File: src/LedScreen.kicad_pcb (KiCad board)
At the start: 2 copper layers, 87 x 84 mm, 38 parts

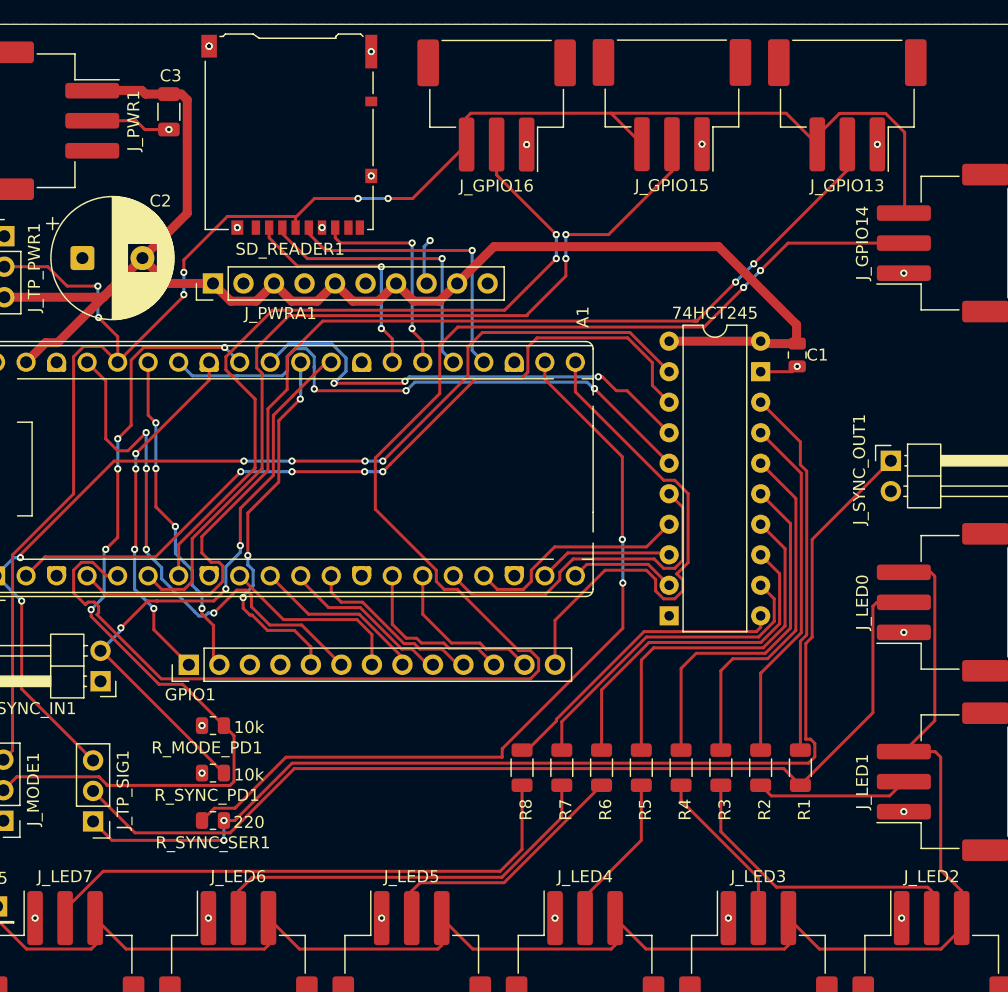
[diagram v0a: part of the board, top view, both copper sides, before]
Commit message: Reorganize KiCad project layout
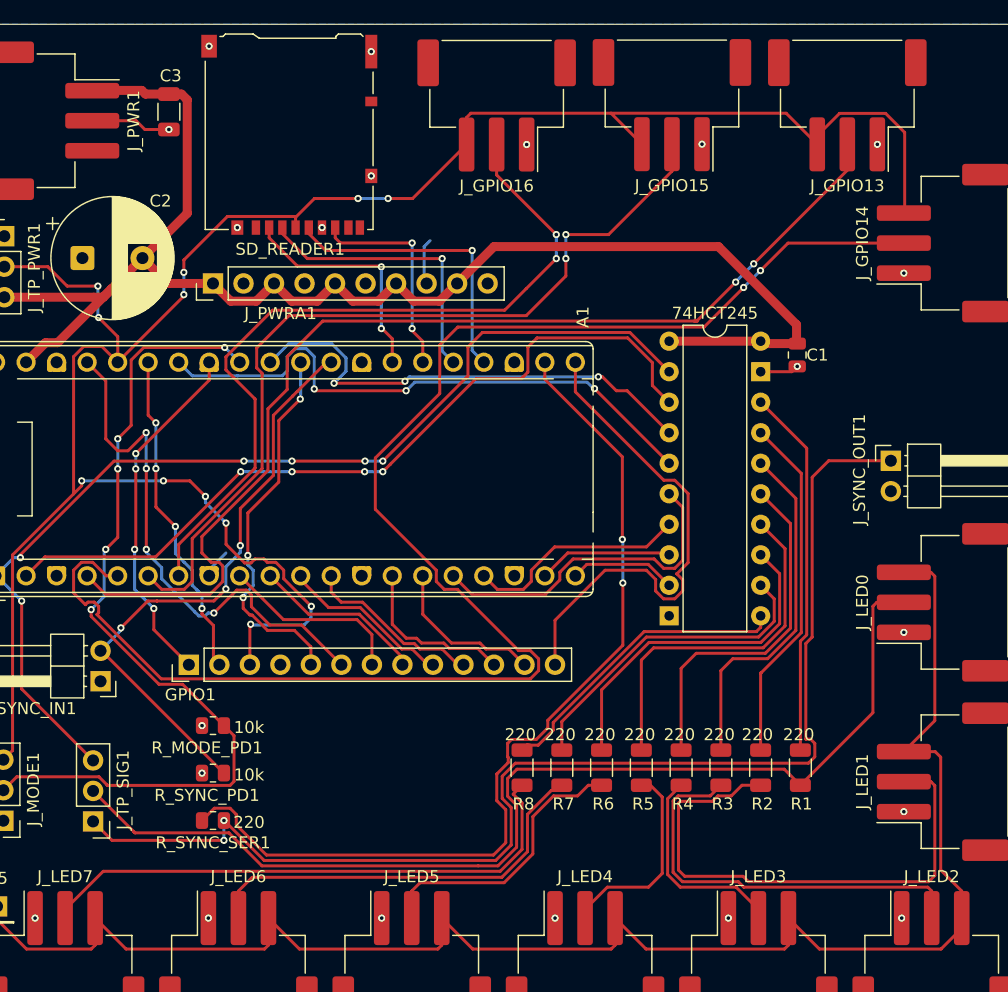
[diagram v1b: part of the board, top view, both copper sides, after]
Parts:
- R1, R2, R3, R4, R5, R6, R7, R8: value 0R -> 220
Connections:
- GPIO1 pad 3: SWCLK -> +3V3
- GPIO1 pad 4: SWDIO -> GND
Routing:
- net +3V3: track 147.7 -> 184.2 mm, vias 6 -> 12
- net LED1_DATA: track 12.8 -> 45.2 mm
- net SYNC_OUT: track 92.8 -> 103.0 mm
- net SYNC_OUT_DRV: track 66.9 -> 76.8 mm
- net LED2_DATA: track 25.7 -> 34.9 mm
- net LED0_DATA: track 83.2 -> 90.0 mm
- net LED4_DATA: track 13.0 -> 16.9 mm
- net LED3_DATA: track 13.7 -> 17.4 mm
- net GND: track 13.9 -> 16.4 mm, vias 23 -> 21
- net LED5_DATA: track 21.7 -> 23.5 mm
- net LED7_DATA: track 46.2 -> 46.8 mm

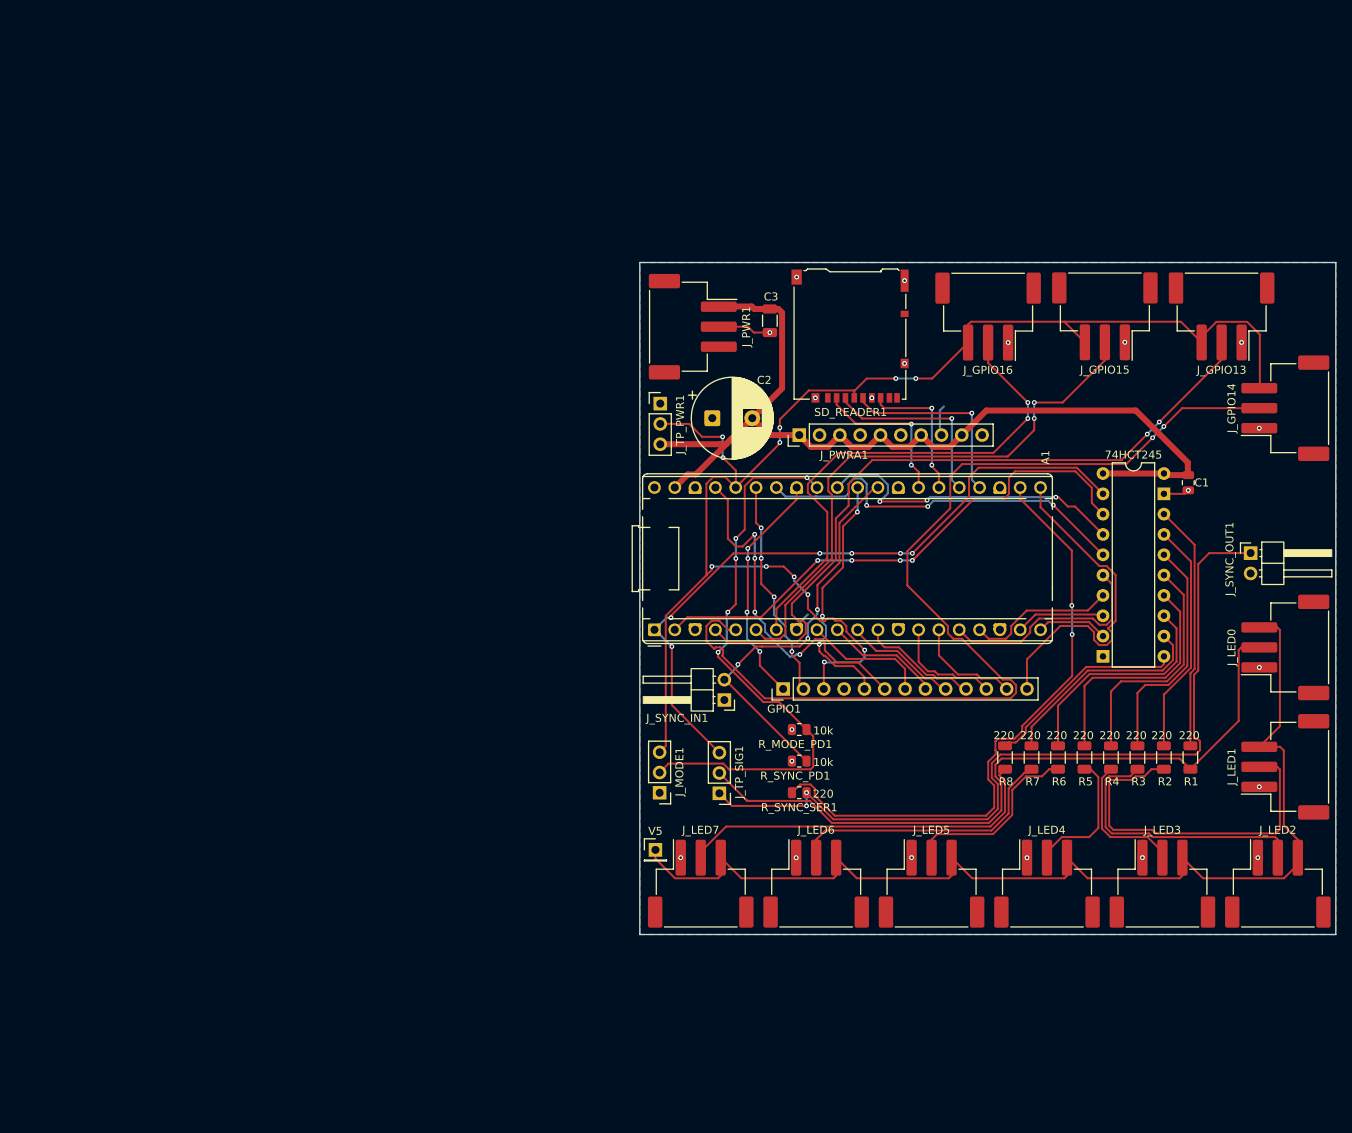
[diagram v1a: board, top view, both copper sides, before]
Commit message: added Bom+Journal
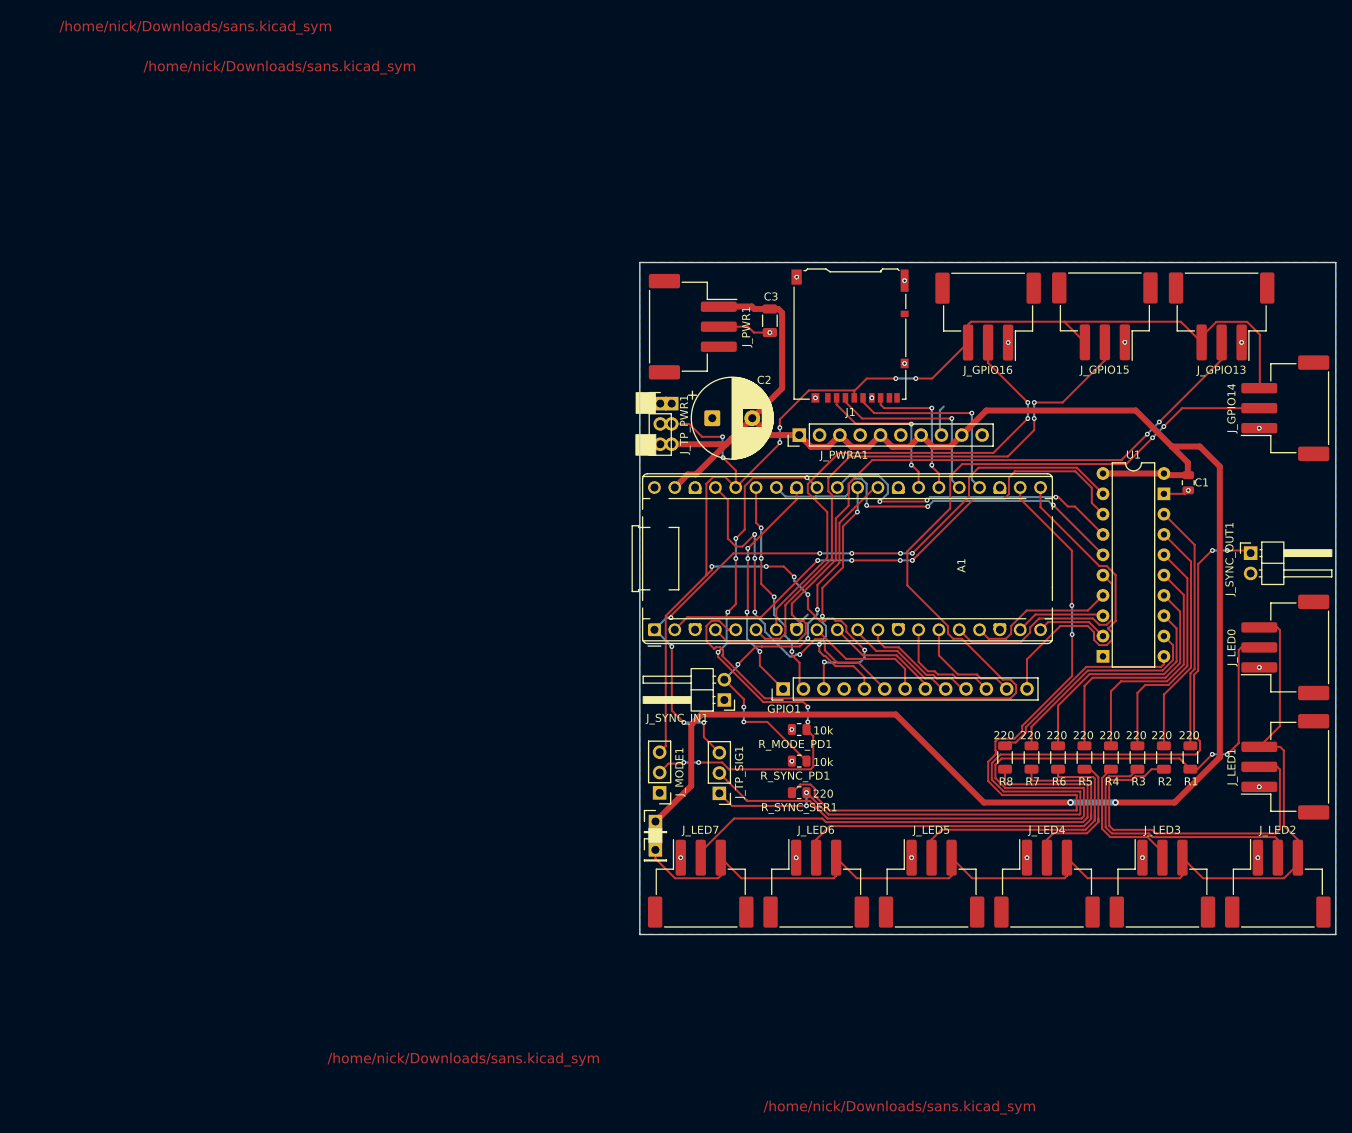
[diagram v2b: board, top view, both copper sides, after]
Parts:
- added ?: , , F.Cu at (91.0, 78.6)
- added ?: , , F.Cu at (91.0, 81.2)
- added ?: , , F.Cu at (91.0, 83.7)
- added V2: Conn_01x01_Pin, Connector_PinHeader_2.54mm:PinHeader_1x01_P2.54mm_Vertical, F.Cu at (89.0, 130.9)
- renumbered SD_READER1 to J1, 74HCT245 to U1
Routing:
- net +5V: track 122.2 -> 253.1 mm, vias 0 -> 2
- net LED0_DATA: track 90.0 -> 112.0 mm, vias 0 -> 2
- net LED7_DATA: track 46.8 -> 67.5 mm
- net SYNC_OUT: track 103.0 -> 123.3 mm, vias 2 -> 4
- net SYNC_OUT_DRV: track 76.8 -> 96.6 mm
- net LED6_DATA: track 34.6 -> 51.8 mm
- net LED5_DATA: track 23.5 -> 35.8 mm
- net MODE: track 72.6 -> 74.5 mm, vias 5 -> 9
- net SYNC_IN: track 49.9 -> 51.7 mm, vias 3 -> 5
- net LED4_DATA: track 16.9 -> 18.5 mm
- net T_OUT0: track 86.6 -> 88.0 mm, vias 6 -> 8
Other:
- board text added: "/home/nick/Downloads/sans.kicad_sym"
- board text added: "Nick Essleman"
- board text added: "Ruben Straks"

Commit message: ITWIRJS
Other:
- board text removed: "/home/nick/Downloads/sans.kicad_sym"
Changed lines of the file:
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@@
 		(layer "Edge.Cuts")
-	)
-	(gr_text "/home/nick/Downloads/sans.kicad_sym"
-		(at 31.5 31.5 0)
-		(layer "F.Cu")
-		(effects
-			(font
-				(size 1.27 1.27)
-			)
-		)
-	)
-	(gr_text "/home/nick/Downloads/sans.kicad_sym"
-		(at 42 36.5 0)
-		(layer "F.Cu")
-		(effects
-			(font
-				(size 1.27 1.27)
-			)
-		)
-	)
-	(gr_text "/home/nick/Downloads/sans.kicad_sym"
-		(at 65 160.5 0)
-		(layer "F.Cu")
-		(effects
-			(font
-				(size 1.27 1.27)
-			)
-		)
-	)
-	(gr_text "/home/nick/Downloads/sans.kicad_sym"
-		(at 119.5 166.5 0)
-		(layer "F.Cu")
-		(effects
-			(font
-				(size 1.27 1.27)
-			)
-		)
 	)
 	(gr_text "Ruben Straks"

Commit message: FIRMWARE DONEE!
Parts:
- moved V5 0.76 mm to (89.0, 133.7)
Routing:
- net LED_PIN3: track 137.0 -> 163.7 mm
- net +5V: track 253.1 -> 254.0 mm
- net LED1_DATA: track 45.2 -> 44.7 mm
- net LED3_DATA: track 17.4 -> 16.9 mm
- net LED2_DATA: track 34.9 -> 34.4 mm

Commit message: Updare README
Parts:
- moved V5 0.16 mm to (89.1, 133.7)
- moved V2 0.16 mm to (89.1, 130.9)
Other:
- board text added: "LED Power"
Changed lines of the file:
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@@
 	(footprint "Connector_PinHeader_2.54mm:PinHeader_1x01_P2.54mm_Vertical"
 		(layer "F.Cu")
-		(at 88.957736 130.87717)
+		(at 89.122075 130.882786)
 		(descr "Through hole straight pin header, 1x01, 2.54mm pitch, single row")
 		(tags "Through hole pin header THT 1x01 2.54mm single row")
@@
 	(footprint "Connector_PinHeader_2.54mm:PinHeader_1x01_P2.54mm_Vertical"
 		(layer "F.Cu")
-		(at 88.961272 133.663471)
+		(at 89.125611 133.669087)
 		(descr "Through hole straight pin header, 1x01, 2.54mm pitch, single row")
 		(tags "Through hole pin header THT 1x01 2.54mm single row")
@@
 	)
 	(gr_rect
-		(start 88.112075 131.211819)
-		(end 89.770115 133.160729)
+		(start 88.276414 131.217435)
+		(end 89.934454 133.166345)
 		(stroke
 			(width 0.1)
@@
 		(layer "Edge.Cuts")
 	)
+	(gr_text "LED Power"
+		(at 87.039272 130.275595 270)
+		(layer "F.SilkS")
+		(effects
+			(font
+				(size 0.5 0.5)
+				(thickness 0.1)
+				(bold yes)
+			)
+			(justify left bottom)
+		)
+	)
 	(gr_text "Ruben Straks"
 		(at 173 66.5 0)
@@
 	)
 	(segment
+		(start 119 117.5)
+		(end 94.690438 117.5)
+		(width 0.75)
+		(layer "F.Cu")
+		(net 1)
+	)
+	(segment
 		(start 103.168031 82.57)
 		(end 101.055 80.456969)
@@
 	)
 	(segment
-		(start 104.781 76.730969)
-		(end 101.055 80.456969)
+		(start 93.426 127.5)
+		(end 90.043214 130.882786)
 		(width 0.75)
 		(layer "F.Cu")
@@
 	)
 	(segment
-		(start 93.426 128.074)
-		(end 90.62283 130.87717)
+		(start 104.781 76.730969)
+		(end 101.055 80.456969)
 		(width 0.75)
 		(layer "F.Cu")
@@
 	)
 	(segment
-		(start 106.925 82.57)
-		(end 103.168031 82.57)
+		(start 130 128.5)
+		(end 119 117.5)
 		(width 0.75)
 		(layer "F.Cu")
@@
 	)
 	(segment
-		(start 93.426 118.764438)
-		(end 93.426 128.074)
+		(start 106.925 82.57)
+		(end 103.168031 82.57)
 		(width 0.75)
 		(layer "F.Cu")
@@
 	)
 	(segment
-		(start 119 117.5)
-		(end 94.690438 117.5)
+		(start 153.5 84)
+		(end 155.5 86)
 		(width 0.75)
 		(layer "F.Cu")
@@
 	)
 	(segment
-		(start 153.5 84)
-		(end 155.5 86)
+		(start 113.481 84.046)
+		(end 115.609 84.046)
 		(width 0.75)
 		(layer "F.Cu")
@@
 	)
 	(segment
-		(start 113.481 84.046)
-		(end 115.609 84.046)
+		(start 93.426 118.764438)
+		(end 93.426 127.5)
 		(width 0.75)
 		(layer "F.Cu")
@@
 	)
 	(segment
-		(start 90.62283 130.87717)
-		(end 88.957736 130.87717)
+		(start 98.494015 83.005985)
+		(end 98.505985 83.005985)
 		(width 0.75)
 		(layer "F.Cu")
@@
 	)
 	(segment
-		(start 98.494015 83.005985)
-		(end 98.505985 83.005985)
+		(start 157 84)
+		(end 153.5 84)
 		(width 0.75)
 		(layer "F.Cu")
@@
 	)
 	(segment
-		(start 157 84)
-		(end 153.5 84)
+		(start 94.690438 117.5)
+		(end 93.426 118.764438)
 		(width 0.75)
 		(layer "F.Cu")
@@
 	)
 	(segment
-		(start 94.690438 117.5)
-		(end 93.426 118.764438)
-		(width 0.75)
-		(layer "F.Cu")
-		(net 1)
-	)
-	(segment
 		(start 108.401 84.046)
 		(end 110.529 84.046)
@@
 	)
 	(segment
-		(start 98.505985 83.005985)
-		(end 101.055 80.456969)
+		(start 90.043214 130.882786)
+		(end 89.122075 130.882786)
 		(width 0.75)
 		(layer "F.Cu")
@@
 	)
 	(segment
-		(start 97.796969 83.715)
-		(end 98.505985 83.005985)
+		(start 98.505985 83.005985)
+		(end 101.055 80.456969)
 		(width 0.75)
 		(layer "F.Cu")
@@
 	)
 	(segment
-		(start 110.529 84.046)
-		(end 112.005 82.57)
+		(start 97.796969 83.715)
+		(end 98.505985 83.005985)
 		(width 0.75)
 		(layer "F.Cu")
@@
 	)
 	(segment
-		(start 130 128.5)
-		(end 119 117.5)
+		(start 110.529 84.046)
+		(end 112.005 82.57)
 		(width 0.75)
 		(layer "F.Cu")
@@
 	)
 	(segment
-		(start 88.961272 133.663471)
-		(end 88.961272 137.961272)
-		(width 0.75)
-		(layer "F.Cu")
-		(net 7)
-	)
-	(segment
 		(start 169.250714 136.249286)
 		(end 169.250714 135.395)
@@
 	)
 	(segment
+		(start 89.125611 137.625611)
+		(end 89.125611 133.669087)
+		(width 0.75)
+		(layer "F.Cu")
+		(net 7)
+	)
+	(segment
 		(start 153.468571 139)
 		(end 150.5 139)
@@
 	)
 	(segment
-		(start 90 139)
-		(end 95.76 139)
-		(width 0.75)
-		(layer "F.Cu")
-		(net 7)
-	)
-	(segment
 		(start 154.823571 137.645)
 		(end 153.468571 139)
@@
 	)
 	(segment
+		(start 90.5 139)
+		(end 95.76 139)
+		(width 0.75)
+		(layer "F.Cu")
+		(net 7)
+	)
+	(segment
 		(start 168.5 123.357143)
 		(end 168.5 124)
@@
 	)
 	(segment
-		(start 88.961272 137.961272)
-		(end 90 139)
+		(start 164.432857 106.612857)
+		(end 166.682857 106.612857)
 		(width 0.75)
 		(layer "F.Cu")
@@
 	)
 	(segment
-		(start 164.432857 106.612857)
-		(end 166.682857 106.612857)
+		(start 90.5 139)
+		(end 89.125611 137.625611)
 		(width 0.75)
 		(layer "F.Cu")

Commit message: FINAL BLOWW! added gerbers added new images, uploaded carts
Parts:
- added G***: LOGO, LOGO, F.Cu at (125.0, 124.0)
- added G***: LOGO, LOGO, B.Cu at (167.5, 72.0)
- added G***: LOGO, LOGO, B.Cu at (118.7, 66.6)
- added G***: LOGO, LOGO, B.Cu at (155.5, 115.0)
- added REF**: MountingHole_3.2mm_M3, MountingHole:MountingHole_3.2mm_M3, F.Cu at (117.0, 123.0)
- added REF**: MountingHole_3.2mm_M3, MountingHole:MountingHole_3.2mm_M3, F.Cu at (169.0, 91.0)
- added REF**: MountingHole_3.2mm_M3, MountingHole:MountingHole_3.2mm_M3, F.Cu at (102.0, 133.0)
- added REF**: MountingHole_3.2mm_M3, MountingHole:MountingHole_3.2mm_M3, F.Cu at (159.5, 133.0)
- added REF**: MountingHole_3.2mm_M3, MountingHole:MountingHole_3.2mm_M3, F.Cu at (122.5, 73.0)
- moved C3 6.73 mm to (98.8, 63.3), turned to 180 degrees
- moved J1 2.50 mm to (110.8, 70.2)
- moved C2 1.00 mm to (95.1, 80.5)
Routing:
- net LED_PIN3: track 163.3 -> 148.1 mm
- net +5V: track 253.5 -> 261.8 mm
- net LED2_DATA: track 34.4 -> 37.5 mm
- net SD_MISO: track 17.7 -> 20.5 mm
- net SD_SCK: track 24.4 -> 27.1 mm
- net LED1_DATA: track 44.7 -> 42.0 mm
- net LED7_DATA: track 67.5 -> 70.0 mm
- net SD_MOSI: track 23.7 -> 26.2 mm
- net SD_CS: track 19.5 -> 22.0 mm
- net +3V3: track 184.2 -> 186.2 mm
- net GND: track 16.4 -> 18.2 mm
- net LED5_DATA: track 35.8 -> 34.5 mm
- net LED3_DATA: track 16.9 -> 17.7 mm
- net LED6_DATA: track 51.8 -> 51.3 mm
